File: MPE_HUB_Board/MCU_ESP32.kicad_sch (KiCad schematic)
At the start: 43 parts, among them J7 PZ254-1-04-Z-2.5-G1, Q1 IRLML0100TRPBF, U3 MAX3485ESA, U4 ESP32-S3-MINI-1-N4R2

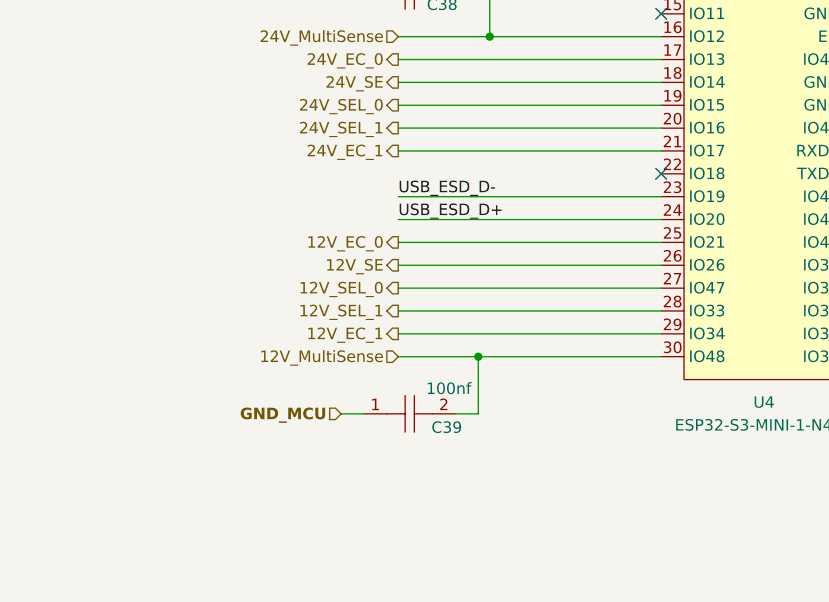
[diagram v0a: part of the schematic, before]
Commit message: Implementazione server e richieste POST/GET
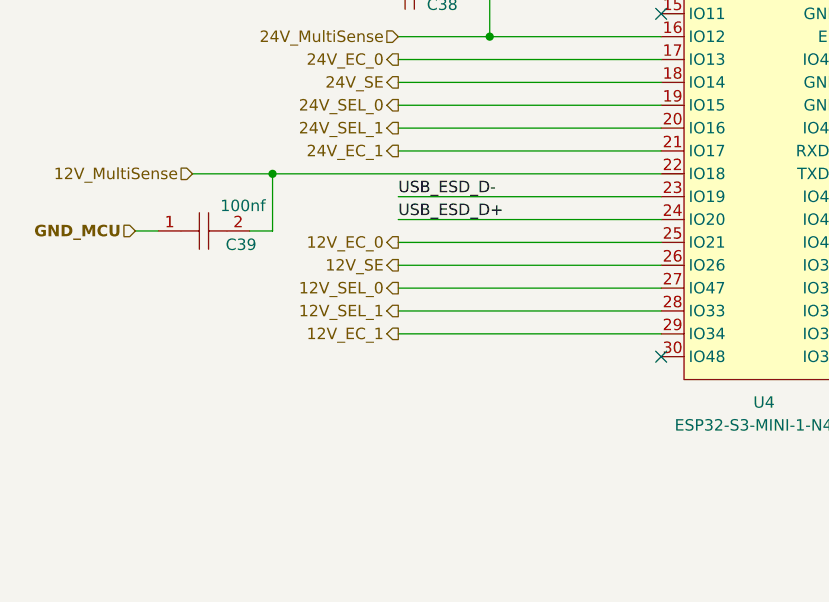
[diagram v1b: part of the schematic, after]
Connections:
- net 12V_MultiSense: now also U4.22 (IO18); no longer U4.30 (IO48)
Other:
- moved on the sheet: C39
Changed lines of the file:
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@@
 	)
 	(junction
-		(at 176.53 173.99)
-		(diameter 0)
-		(color 0 0 0 0)
-	)
-	(junction
 		(at 222.25 123.19)
 		(diameter 0)
@@
 	)
 	(junction
+		(at 153.67 153.67)
+		(diameter 0)
+		(color 0 0 0 0)
+	)
+	(junction
 		(at 222.25 115.57)
 		(diameter 0)
@@
 	)
 	(no_connect
-		(at 196.85 153.67)
+		(at 219.71 140.97)
 	)
 	(no_connect
-		(at 219.71 140.97)
+		(at 196.85 173.99)
 	)
 	(no_connect
@@
 	(wire
 		(pts
-			(xy 176.53 173.99) (xy 176.53 180.34)
+			(xy 153.67 153.67) (xy 196.85 153.67)
 		)
 		(stroke
@@
 	(wire
 		(pts
-			(xy 161.29 180.34) (xy 163.83 180.34)
-		)
-		(stroke
-			(width 0)
-			(type default)
-		)
-	)
-	(wire
-		(pts
 			(xy 308.61 40.64) (xy 334.01 40.64)
 		)
@@
 	(wire
 		(pts
-			(xy 167.64 173.99) (xy 176.53 173.99)
-		)
-		(stroke
-			(width 0)
-			(type default)
-		)
-	)
-	(wire
-		(pts
 			(xy 351.79 40.64) (xy 355.6 40.64)
 		)
@@
 	(wire
 		(pts
+			(xy 144.78 153.67) (xy 153.67 153.67)
+		)
+		(stroke
+			(width 0)
+			(type default)
+		)
+	)
+	(wire
+		(pts
 			(xy 186.69 125.73) (xy 196.85 125.73)
 		)
@@
 	(wire
 		(pts
-			(xy 176.53 173.99) (xy 196.85 173.99)
+			(xy 153.67 153.67) (xy 153.67 160.02)
 		)
 		(stroke
@@
 	(wire
 		(pts
-			(xy 176.53 180.34) (xy 173.99 180.34)
+			(xy 153.67 160.02) (xy 151.13 160.02)
 		)
 		(stroke
@@
 		)
 	)
+	(wire
+		(pts
+			(xy 138.43 160.02) (xy 140.97 160.02)
+		)
+		(stroke
+			(width 0)
+			(type default)
+		)
+	)
 	(label "USB_D-"
 		(at 381 204.47 180)
@@
 	(hierarchical_label "GND_MCU"
 		(shape input)
-		(at 161.29 180.34 180)
-		(effects
-			(font
-				(size 1.27 1.27)
-				(thickness 0.254)
-				(bold yes)
-				(color 0 0 0 1)
-			)
-			(justify right)
-		)
-	)
-	(hierarchical_label "GND_MCU"
-		(shape input)
 		(at 236.22 100.33 0)
 		(effects
@@
 		)
 	)
-	(hierarchical_label "12V_MultiSense"
-		(shape input)
-		(at 167.64 173.99 180)
-		(effects
-			(font
-				(size 1.27 1.27)
-				(color 0 0 194 1)
-			)
-			(justify right)
-		)
-	)
 	(hierarchical_label "3V3_MCU"
 		(shape input)
@@
 	(hierarchical_label "GND_MCU"
 		(shape input)
+		(at 138.43 160.02 180)
+		(effects
+			(font
+				(size 1.27 1.27)
+				(thickness 0.254)
+				(bold yes)
+				(color 0 0 0 1)
+			)
+			(justify right)
+		)
+	)
+	(hierarchical_label "12V_MultiSense"
+		(shape input)
+		(at 144.78 153.67 180)
+		(effects
+			(font
+				(size 1.27 1.27)
+				(color 0 0 194 1)
+			)
+			(justify right)
+		)
+	)
+	(hierarchical_label "GND_MCU"
+		(shape input)
 		(at 261.62 274.32 180)
 		(effects
@@
 		(lib_name "CC0603KRX7R9BB104_2")
 		(lib_id "easyeda2kicad:CC0603KRX7R9BB104")
-		(at 168.91 180.34 0)
+		(at 146.05 160.02 0)
 		(unit 1)
 		(exclude_from_sim no)
@@
 		(dnp no)
 		(property "Reference" "C39"
-			(at 174.752 181.864 0)
+			(at 151.892 161.544 0)
 			(effects
 				(font
@@
 		)
 		(property "Value" "100nf"
-			(at 175.768 177.546 0)
+			(at 152.908 157.226 0)
 			(effects
 				(font
@@
 		)
 		(property "Footprint" "Capacitor_SMD:C_0603_1608Metric"
-			(at 168.91 187.96 0)
+			(at 146.05 167.64 0)
 			(effects
 				(font
@@
 		)
 		(property "Datasheet" "https://lcsc.com/product-detail/Multilayer-Ceramic-Capacitors-MLCC-SMD-SMT_100nF-104-10-50V_C14663.html"
-			(at 168.91 190.5 0)
+			(at 146.05 170.18 0)
 			(effects
 				(font
@@
 		)
 		(property "Description" ""
-			(at 168.91 180.34 0)
+			(at 146.05 160.02 0)
 			(effects
 				(font
@@
 		)
 		(property "LCSC Part" "C14663"
-			(at 168.91 193.04 0)
+			(at 146.05 172.72 0)
 			(effects
 				(font
@@
 		)
 		(property "LCSC" "C14663"
-			(at 171.45 182.245 0)
+			(at 148.59 161.925 0)
 			(effects
 				(font

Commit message: Versione WiFi completa
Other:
- note added: "SPOSTARE SENS ENABLE SU IO 48"
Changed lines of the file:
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@@
+		)
+	)
+	(text "SPOSTARE SENS ENABLE SU IO 48"
+		(exclude_from_sim no)
+		(at 177.038 177.8 0)
+		(effects
+			(font
+				(size 1.27 1.27)
+			)
 		)
 	)

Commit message: Versione WiFi + Ethernet (04/06/2025)
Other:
- note added: "IO45 E IO46 VIETATI IO26 VIETATO NELLA CONFIGURAZIONE N4R2 (PSRAM)"
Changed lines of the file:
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@@
+		)
+	)
+	(text "IO45 E IO46 VIETATI\nIO26 VIETATO NELLA CONFIGURAZIONE N4R2 (PSRAM)"
+		(exclude_from_sim no)
+		(at 17.018 19.304 0)
+		(effects
+			(font
+				(size 2 2)
+				(thickness 0.4)
+				(bold yes)
+			)
+			(justify left)
 		)
 	)

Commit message: update 11/06/2025
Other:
- note added: "AGGIUNGERE PARTITORE SUL MULTISENSE"
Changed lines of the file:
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@@
 			(font
 				(size 1.27 1.27)
+				(thickness 0.254)
+				(bold yes)
+				(color 194 0 194 1)
 			)
 		)
@@
 		)
 	)
+	(text "AGGIUNGERE PARTITORE SUL MULTISENSE"
+		(exclude_from_sim no)
+		(at 130.302 150.622 0)
+		(effects
+			(font
+				(size 1.27 1.27)
+				(thickness 0.254)
+				(bold yes)
+				(color 194 0 194 1)
+			)
+		)
+	)

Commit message: Risolto problema reset (Nel firmware V2)
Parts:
- added C69: 100nf, Capacitor_SMD:C_0603_1608Metric, symbol easyeda2kicad:CC0603KRX7R9BB104
- added JP4: SolderJumper_2_Open, Jumper:SolderJumper-2_P1.3mm_Open_RoundedPad1.0x1.5mm, symbol Jumper:SolderJumper_2_Open
- added LED20: 0805_RED, easyeda2kicad:LED0805-R-RD, symbol easyeda2kicad:FC-2012HRK-620D
- added LED21: 0805_GREEN, easyeda2kicad:LED0805-R-RD, symbol easyeda2kicad:0805G(Green)
- added R105: 300, Resistor_SMD:R_0603_1608Metric, symbol Device:R
- added R106: 100k, Resistor_SMD:R_0603_1608Metric, symbol Device:R
- added R107: 220, Resistor_SMD:R_0603_1608Metric, symbol Device:R
- added R108, R109: 0, Resistor_SMD:R_0603_1608Metric, symbol Device:R
- added R110, R112: 10K, Resistor_SMD:R_0603_1608Metric, symbol Device:R
- added R111: 120, Resistor_SMD:R_0603_1608Metric, symbol Device:R
- added U8: MAX3485ESA, easyeda2kicad:SOP-8_L5.0-W4.0-P1.27-LS6.0-BL, symbol easyeda2kicad:MAX3485ESA
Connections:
- net 12V_SE: now also U4.30 (IO48); no longer U4.26 (IO26)
- net 3V3_MCU: now also C69.2, LED20.1 (+), LED21.1 (A), R112.2, U8.8 (VCC)
- net GND_MCU: now also C69.1, R106.2, R110.1, U8.5 (GND)
- net RX1_485_ROV: now reaches U4.36 (IO40)
- net RX1_485_ROV: now also R105.1, U8.1 (RO)
- net R/W_485_ROV: now reaches U4.37 (IO41)
- net R/W_485_ROV: now also R106.1, U8.2 (#RE), U8.3 (DE)
- net TX1_485_ROV: now reaches U4.38 (IO42)
- net TX1_485_ROV: now also R107.1, U8.4 (DI)
- net 485A renamed 485_LED_A
- net 485B renamed 485_LED_B
- net RX2_485 renamed RX2_485_LED
- net R/W_485 renamed R/W_485_LED
- net TX2_485 renamed TX2_485_LED
- new net: R109.1, U8.6 (A)
- new net: R108.1, U8.7 (B)
- new net: JP4.1 (A), R111.1
- new net: LED21.2 (K), R107.2
- new net: LED20.2 (-), R105.2
- new net 485_ROV_A: R109.2, R111.2, R112.1
- new net 485_ROV_B: JP4.2 (B), R108.2, R110.2
- no-connect marks 14 -> 11
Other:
- note added: "IO45 E IO46 VIETATI (in alcuni casi rientrano negli strapping pin) IO26 VIETATO NELLA CONFIGURAZIONE N4R2 (PSRAM)"
- note removed: "IO45 E IO46 VIETATI IO26 VIETATO NELLA CONFIGURAZIONE N4R2 (PSRAM)"
- note removed: "SPOSTARE SENS ENABLE SU IO 48"
- company: (none) -> 3DResearch
- title: (none) -> ESP32 MCU
- moved on the sheet: C38, C39, U4

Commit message: Update 04/07/2025
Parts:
- removed R108, R109, R26, R31: 0, Resistor_SMD:R_0603_1608Metric, symbol Device:R
- added C70, C71: 100nf, Capacitor_SMD:C_0603_1608Metric, symbol easyeda2kicad:CC0603KRX7R9BB104
- added JP5: SolderJumper_2_Open, Jumper:SolderJumper-2_P1.3mm_Open_RoundedPad1.0x1.5mm, symbol Jumper:SolderJumper_2_Open
- added LED22: 0805_RED, easyeda2kicad:LED0805-R-RD, symbol easyeda2kicad:FC-2012HRK-620D
- added LED23: 0805_GREEN, easyeda2kicad:LED0805-R-RD, symbol easyeda2kicad:0805G(Green)
- added R108, R109, R26, R31, R93, R94: CRCW060310R0JNEAHP, easyeda2kicad:R0603, symbol easyeda2kicad:CRCW060310R0JNEAHP
- added R85, R86, R89, R95, R97: 10K, Resistor_SMD:R_0603_1608Metric, symbol Device:R
- added R90, R92: 1K, Resistor_SMD:R_0603_1608Metric, symbol Device:R
- added R91: 100k, Resistor_SMD:R_0603_1608Metric, symbol Device:R
- added R96: 120, Resistor_SMD:R_0603_1608Metric, symbol Device:R
- added U10: MAX3485ESA, easyeda2kicad:SOP-8_L5.0-W4.0-P1.27-LS6.0-BL, symbol easyeda2kicad:MAX3485ESA
- added U9: ADS1015IDGSR, easyeda2kicad:VSSOP-10_L3.0-W3.0-P0.50-LS4.9-BL, symbol easyeda2kicad:ADS1015IDGSR
- J7: now fitted; now in the parts list
- R105, R28: value 300 -> 1K; LCSC C23025 -> C21190; LCSC Part C23025 -> C21190
- R107, R30: value 220 -> 1K; LCSC C22962 -> C21190; LCSC Part C22962 -> C21190
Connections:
- net 24V_SE is gone; now on net 24V_EC_0: U4.18 (IO14)
- net 12V_EC_1: now also U4.22 (IO18); no longer U4.29 (IO34)
- net 12V_MultiSense: no longer U4.22 (IO18)
- net 24V_EC_0: no longer U4.17 (IO13)
- net 24V_MultiSense: no longer U4.16 (IO12)
- net 3V3_MCU: now also C70.2, C71.2, LED22.1 (+), LED23.1 (A), R85.1, R86.1, R89.1, R97.2, U10.8 (VCC), U9.8 (VDD)
- net 485_ROV_A: now also R109.2
- net 485_ROV_B: now also R108.2
- net GND_MCU: now also C70.1, C71.1, R91.2, R95.1, U10.5 (GND), U9.3 (GND)
- net RX1_485_ROV: now also R105.2; no longer R105.1
- net TX1_485_ROV: now also R107.2; no longer R107.1
- net at U8.6 (A): now also R109.1
- net at U8.7 (B): now also R108.1
- net TX3_485_LED2: now reaches U4.15 (IO11)
- net TX3_485_LED2: now also R30.2, U3.4 (DI)
- net CONV_RDY: now reaches U4.5 (IO1)
- net CONV_RDY: now also R89.2, U9.2 (ALERT/RDY)
- net at U3.7 (B): now also R26.1
- net at LED10.2 (K): now also R30.1; no longer R30.2
- net at U3.6 (A): now also R31.1
- net at LED9.2 (-): now also R28.1; no longer R28.2
- net at LED21.2 (K): now also R107.1; no longer R107.2
- net at LED20.2 (-): now also R105.1; no longer R105.2
- net 12V_SE renamed SCL
- net SCL: now also U9.1 (ADDR), U9.10 (SCL)
- net 485_LED_A renamed 485_LED2_A
- net 485_LED2_A: now also R31.2
- net 485_LED_B renamed 485_LED2_B
- net 485_LED2_B: now also R26.2
- removed net RX2_485_LED: R28.1, U3.1 (RO), U4.8 (IO4)
- net R/W_485_LED renamed R/W_485_LED2
- net R/W_485_LED2: now also U4.16 (IO12); no longer U4.7 (IO3)
- removed net TX2_485_LED: R30.1, U3.4 (DI), U4.6 (IO2)
- new net: LED22.2 (-), R90.1
- new net: LED23.2 (K), R92.1
- new net: JP5.1 (A), R96.1
- new net: R94.1, U10.6 (A)
- new net: R93.1, U10.7 (B)
- new net 485_LED1_A: R94.2, R96.2, R97.1
- new net 485_LED1_B: JP5.2 (B), R93.2, R95.2
- new net RX2_485_LED1: R90.2, U10.1 (RO), U4.8 (IO4)
- new net RX3_485_LED2: R28.2, U3.1 (RO), U4.17 (IO13)
- new net R/W_485_LED1: R91.1, U10.2 (#RE), U10.3 (DE), U4.7 (IO3)
- new net SDA: R85.2, R86.2, U4.29 (IO34), U9.9 (SDA)
- new net TX2_485_LED1: R92.2, U10.4 (DI), U4.6 (IO2)
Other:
- note added: "ADDRESS I2C: 1001011"
- note added: "IO45 E IO46 VIETATI (in alcuni casi rientrano negli strapping pin) IO26 VIETATO NELLA CONFIGURAZIONE N4R2 (PSRAM) [IO19 -> USB-] & [IO20 -> USB+]"
- note removed: "IO45 E IO46 VIETATI (in alcuni casi rientrano negli strapping pin) IO26 VIETATO NELLA CONFIGURAZIONE N4R2 (PSRAM)"
- moved on the sheet: C37, C38, C39, C41, C42, C43, C44, C45, C46, C47, C69, JP1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

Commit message: Update 08/07/2025
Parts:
- removed C38, C39: 100nf, Capacitor_SMD:C_0603_1608Metric, symbol easyeda2kicad:CC0603KRX7R9BB104
- removed J7: PZ254-1-04-Z-2.5-G1, easyeda2kicad:HDR-TH_4P-P2.54-V-M, symbol easyeda2kicad:PZ254-1-04-Z-2.5-G1
- removed USB1: TYPEC-304-ACP16, easyeda2kicad:USB-C-SMD_TYPE-C-16P-1, symbol easyeda2kicad:TYPEC-304-ACP16
- added C72: TAJA106K016RNJ, easyeda2kicad:CAP-SMD_L3.2-W1.6-RD-C7171, symbol easyeda2kicad:TAJA106K016RNJ
- added C73: TAJA226M010RNJ, easyeda2kicad:CASE-A_3216, symbol easyeda2kicad:TAJA226M010RNJ
- added D3: 1N5819WS, Diode_SMD:D_SOD-323, symbol Diode:1N5819WS
- added JP6: SolderJumper_2_Bridged, Jumper:SolderJumper-2_P1.3mm_Bridged_RoundedPad1.0x1.5mm, symbol Jumper:SolderJumper_2_Bridged
- added U11: AMS1117-3.3, Package_TO_SOT_SMD:SOT-223-3_TabPin2, symbol Regulator_Linear:AMS1117-3.3
- added USB2: TYPEC-303-ACP16, easyeda2kicad:USB-C-SMD_TYPEC-303-ACP16, symbol easyeda2kicad:TYPEC-303-ACP16
- R37, R38: now fitted; now in the parts list
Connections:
- net 12V_MultiSense: now also U9.4 (AIN0)
- net 24V_MultiSense: now also U9.5 (AIN1)
- net 3V3_MCU: now also JP6.2 (B)
- net GND_MCU: now also C40.2, C72.2, C73.2, U11.1 (GND), USB2.1 (GND), USB2.2 (GND), USB2.3 (GND), USB2.4 (GND), USB2.A1 (GND), USB2.A12 (GND), USB2.B1 (GND), USB2.B12 (GND); no longer C40.1
- net USB_D+: now also USB2.A6 (DP1), USB2.B6 (DP2)
- net USB_D-: now also USB2.A7 (DN1), USB2.B7 (DN2)
- net USB_VBUS: now also C40.1, D3.2 (A), USB2.A4 (VBUS), USB2.A9 (VBUS), USB2.B4 (VBUS), USB2.B9 (VBUS); no longer C40.2
- net at R37.1: now also USB2.A5 (CC1)
- net at R38.1: now also USB2.B5 (CC2)
- new net: C73.1, JP6.1 (A), U11.2 (VO)
- new net: C72.1, D3.1 (K), U11.3 (VI)
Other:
- note removed: "AGGIUNGERE PARTITORE SUL MULTISENSE"
- note removed: "Porta USB non montata ma connessione con PAD"
- moved on the sheet: C40, C44, C45, C46, C47, C70, D2, JP2, JP3, R39, R40, R89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

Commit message: HUB Hardware V1.1.0
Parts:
- removed JP1, JP4, JP5: SolderJumper_2_Open, Jumper:SolderJumper-2_P1.3mm_Open_RoundedPad1.0x1.5mm, symbol Jumper:SolderJumper_2_Open
- removed R110, R112: 10K, Resistor_SMD:R_0603_1608Metric, symbol Device:R
- added C38, C39: 100nf, Capacitor_SMD:C_0603_1608Metric, symbol easyeda2kicad:CC0603KRX7R9BB104
- added R102, R103, R104: 0, Resistor_SMD:R_0603_1608Metric, symbol Device:R
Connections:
- net 12V_MultiSense: now also C38.2
- net 24V_EC_0: now also U4.21 (IO17); no longer U4.18 (IO14)
- net 24V_EC_1: now also U4.18 (IO14); no longer U4.21 (IO17)
- net 24V_MultiSense: now also C39.2
- net 24V_SEL_0: now also U4.20 (IO16); no longer U4.19 (IO15)
- net 24V_SEL_1: now also U4.19 (IO15); no longer U4.20 (IO16)
- net 485_LED1_B: now also R103.1
- net 485_LED2_B: now also R102.1
- net RX2_485_LED1: now also U4.6 (IO2); no longer U4.8 (IO4)
- net SCL: now also R86.2
- net SDA: no longer R86.2
- net TX2_485_LED1: now also U4.8 (IO4); no longer U4.6 (IO2)
- net at R111.1: now also R104.2
- net at R96.1: now also R103.2
- net at R27.1: now also R102.2
- new net GND: C38.1, C39.1
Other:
- moved on the sheet: C70, R89, U9
